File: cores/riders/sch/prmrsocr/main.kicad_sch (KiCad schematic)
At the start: 31 parts

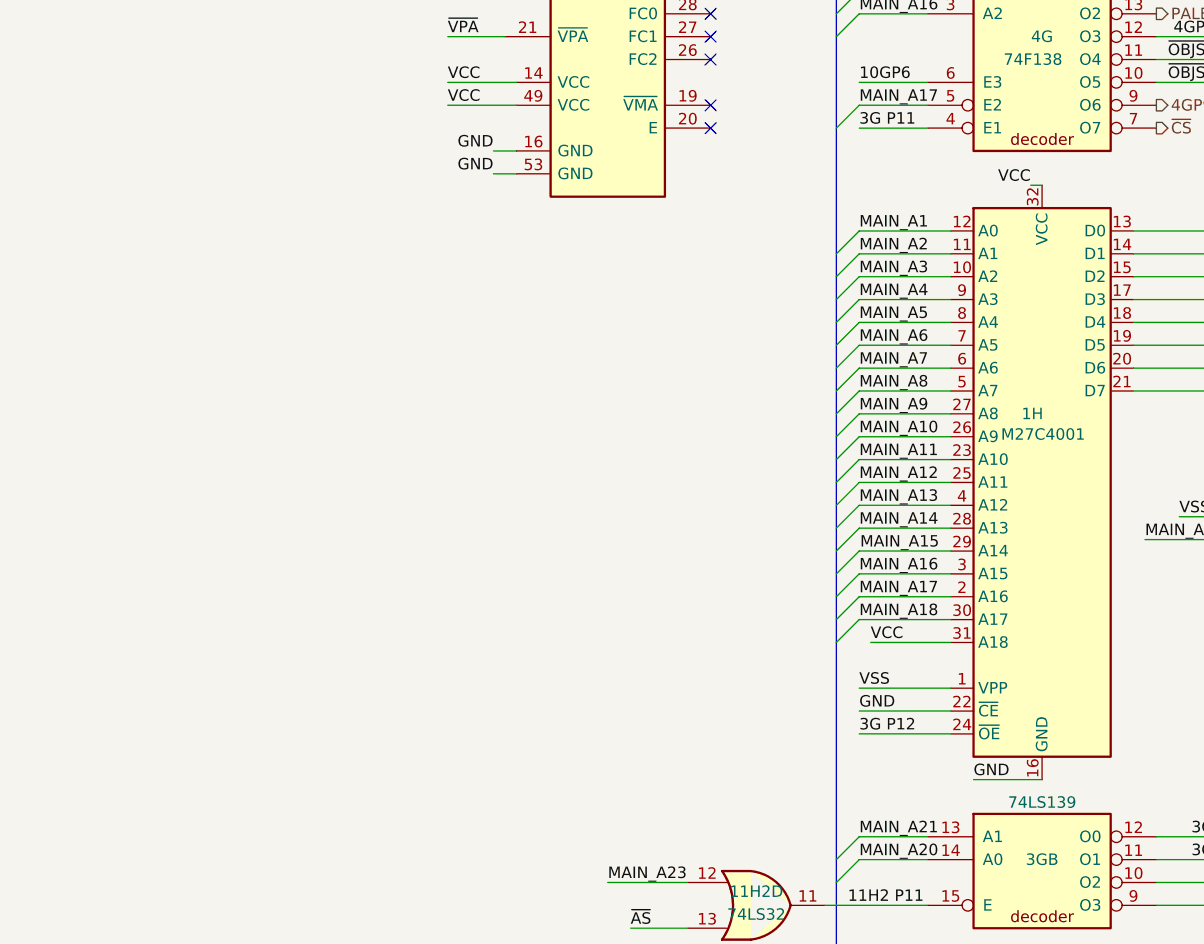
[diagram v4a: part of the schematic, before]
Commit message: prmrsocr sch: finish remove errors
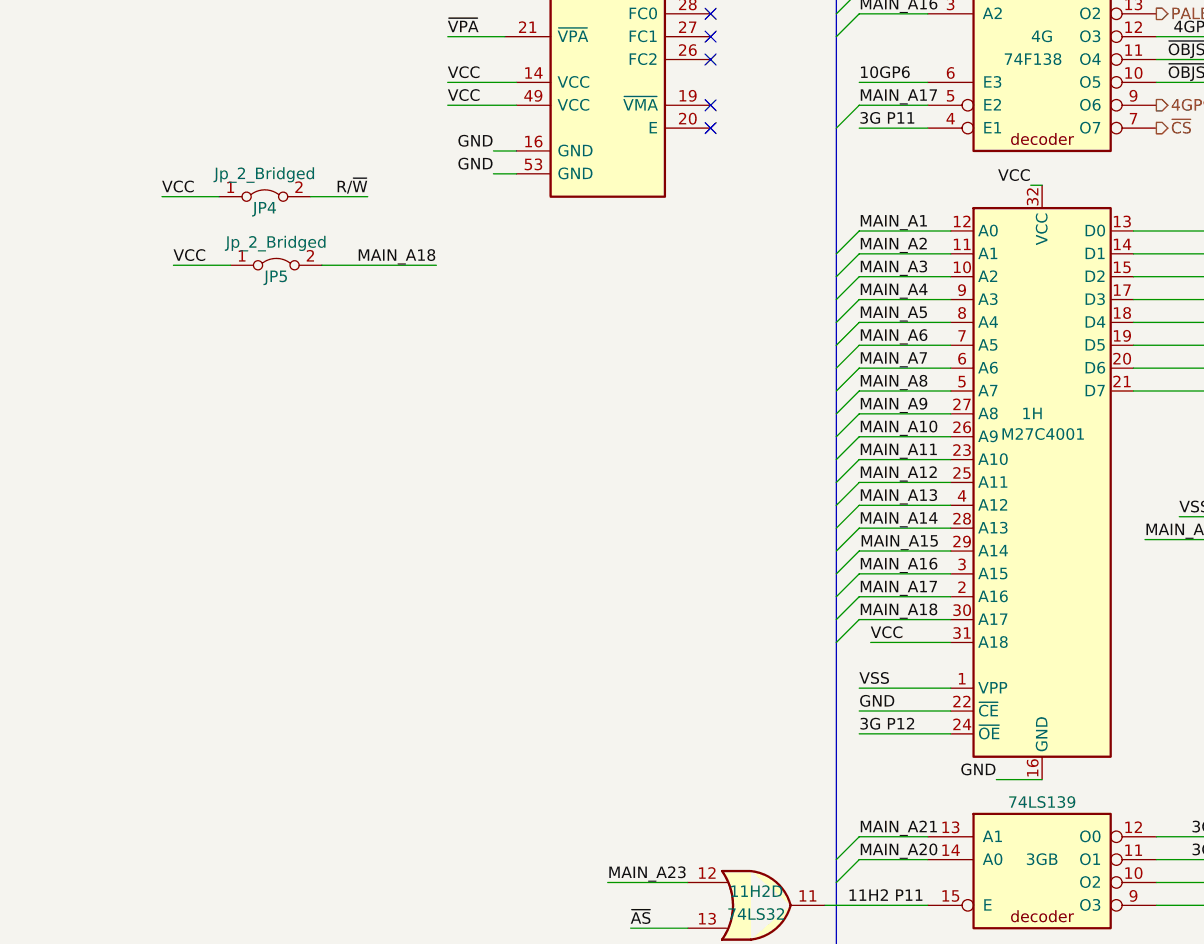
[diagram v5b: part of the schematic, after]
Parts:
- added JP4, JP5: Jp_2_Bridged, symbol Jumper:Jumper_2_Bridged
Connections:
- net MAIN_A18: now also JP5.2 (B)
- net R/~{W}: now also JP4.2 (B)
- net VCC: now also JP4.1 (A), JP5.1 (A)
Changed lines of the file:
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@@
 	(wire
 		(pts
+			(xy 280.67 132.08) (xy 267.97 132.08)
+		)
+		(stroke
+			(width 0)
+			(type default)
+		)
+	)
+	(wire
+		(pts
 			(xy 210.82 52.07) (xy 203.2 52.07)
 		)
@@
 		)
 	)
+	(wire
+		(pts
+			(xy 250.19 124.46) (xy 256.54 124.46)
+		)
+		(stroke
+			(width 0)
+			(type default)
+		)
+	)
 	(bus
 		(pts
@@
 	(wire
 		(pts
-			(xy 340.36 189.23) (xy 347.98 189.23)
-		)
-		(stroke
-			(width 0)
-			(type default)
-		)
-	)
-	(wire
-		(pts
 			(xy 273.05 45.72) (xy 288.29 45.72)
 		)
@@
 	(wire
 		(pts
+			(xy 273.05 124.46) (xy 266.7 124.46)
+		)
+		(stroke
+			(width 0)
+			(type default)
+		)
+	)
+	(wire
+		(pts
 			(xy 43.18 81.28) (xy 53.34 81.28)
 		)
@@
 		)
 	)
+	(wire
+		(pts
+			(xy 251.46 132.08) (xy 257.81 132.08)
+		)
+		(stroke
+			(width 0)
+			(type default)
+		)
+	)
 	(bus
 		(pts
@@
 	(wire
 		(pts
+			(xy 342.9 189.23) (xy 347.98 189.23)
+		)
+		(stroke
+			(width 0)
+			(type default)
+		)
+	)
+	(wire
+		(pts
 			(xy 337.82 148.59) (xy 327.66 148.59)
 		)
@@
 		)
 	)
+	(label "VCC"
+		(at 250.19 124.46 0)
+		(effects
+			(font
+				(size 1.27 1.27)
+			)
+			(justify left bottom)
+		)
+	)
 	(label "MAIN_A7"
 		(at 157.48 231.14 0)
@@
 		)
 	)
-	(label "GND"
-		(at 340.36 189.23 0)
+	(label "MAIN_D5"
+		(at 43.18 161.29 0)
 		(effects
 			(font
@@
 		)
 	)
-	(label "MAIN_D5"
-		(at 43.18 161.29 0)
+	(label "VCC"
+		(at 251.46 132.08 0)
 		(effects
 			(font
@@
 		)
 	)
+	(label "MAIN_A18"
+		(at 280.67 132.08 180)
+		(effects
+			(font
+				(size 1.27 1.27)
+			)
+			(justify right bottom)
+		)
+	)
 	(label "MAIN_A16"
 		(at 327.66 166.37 0)
@@
 		)
 	)
+	(label "R{slash}~{W}"
+		(at 273.05 124.46 180)
+		(effects
+			(font
+				(size 1.27 1.27)
+			)
+			(justify right bottom)
+		)
+	)
 	(label "VSS"
 		(at 260.35 250.19 0)
@@
 		)
 	)
+	(label "GND"
+		(at 342.9 189.23 180)
+		(effects
+			(font
+				(size 1.27 1.27)
+			)
+			(justify right bottom)
+		)
+	)
 	(label "~{HALT}"
 		(at 280.67 88.9 0)
@@
 	)
 	(symbol
+		(lib_id "Jumper:Jumper_2_Bridged")
+		(at 261.62 124.46 0)
+		(unit 1)
+		(exclude_from_sim no)
+		(in_bom yes)
+		(on_board yes)
+		(dnp no)
+		(property "Reference" "JP4"
+			(at 261.62 125.73 0)
+			(effects
+				(font
+					(size 1.27 1.27)
+				)
+			)
+		)
+		(property "Value" "Jp_2_Bridged"
+			(at 261.62 121.92 0)
+			(effects
+				(font
+					(size 1.27 1.27)
+				)
+			)
+		)
+		(property "Footprint" ""
+			(at 261.62 124.46 0)
+			(effects
+				(font
+					(size 1.27 1.27)
+				)
+				(hide yes)
+			)
+		)
+		(property "Datasheet" "~"
+			(at 261.62 124.46 0)
+			(effects
+				(font
+					(size 1.27 1.27)
+				)
+				(hide yes)
+			)
+		)
+		(property "Description" ""
+			(at 261.62 124.46 0)
+			(effects
+				(font
+					(size 1.27 1.27)
+				)
+				(hide yes)
+			)
+		)
+		(pin "1"
+		)
+		(pin "2"
+		)
+		(instances
+			(project "prmrsocr"
+				(path "/0011ec10-82c4-4039-b424-337480f568e8/7d4ab3ba-37fa-4111-bbdb-c99f1a708a52"
+					(reference "JP4")
+					(unit 1)
+				)
+			)
+		)
+	)
+	(symbol
 		(lib_id "Memory_EPROM:27C040")
 		(at 347.98 60.96 0)
@@
 				)
 			)
+		)
+	)
+	(symbol
+		(lib_id "Jumper:Jumper_2_Bridged")
+		(at 262.89 132.08 0)
+		(unit 1)
+		(exclude_from_sim no)
+		(in_bom yes)
+		(on_board yes)
+		(dnp no)
+		(property "Reference" "JP5"
+			(at 262.89 133.35 0)
+			(effects
+				(font
+					(size 1.27 1.27)
+				)
+			)
+		)
+		(property "Value" "Jp_2_Bridged"
+			(at 262.89 129.54 0)
+			(effects
+				(font
+					(size 1.27 1.27)
+				)
+			)
+		)
+		(property "Footprint" ""
+			(at 262.89 132.08 0)
+			(effects
+				(font
+					(size 1.27 1.27)
+				)
+				(hide yes)
+			)
+		)
+		(property "Datasheet" "~"
+			(at 262.89 132.08 0)
+			(effects
+				(font
+					(size 1.27 1.27)
+				)
+				(hide yes)
+			)
+		)
+		(property "Description" ""
+			(at 262.89 132.08 0)
+			(effects
+				(font
+					(size 1.27 1.27)
+				)
+				(hide yes)
+			)
+		)
+		(pin "1"
+		)
+		(pin "2"
+		)
+		(instances
+			(project "prmrsocr"
+				(path "/0011ec10-82c4-4039-b424-337480f568e8/7d4ab3ba-37fa-4111-bbdb-c99f1a708a52"
+					(reference "JP5")
+					(unit 1)
+				)
+			)

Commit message: prmrsocr sch corrections
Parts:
- removed 13H, 14H: 74LS245, symbol jt74:74LS245
- removed 15A: ER5911, symbol arcade:ER5911
- removed 15C2: 74LS174, symbol jt74:74LS174
- removed 16C: 74LS273, symbol jt74:74LS273
- removed 7E1: 74LS32, symbol jt74:74LS32
- removed unit 1 of 7G
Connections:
- net 3G P12 renamed ~{ROM_CS}
- net 3GA P4 renamed 3GP4
- net 4GP15 renamed ~{RAM_CS}
- net 4GP9 renamed ~{NWCS}
- net 7E2 P13 renamed 7E2P13
- net ~{CS} renamed ~{PCU_CS}
- net ~{P1401} renamed ~{OBJ_CS}
- no-connect marks 28 -> 22
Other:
- moved on the sheet: 10GC, 10GE, 11G1C, 11G1D, 11H1A, 11H1B, 11H2D, 12HB, 12HD, 15H2D, 16HA, 16HB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

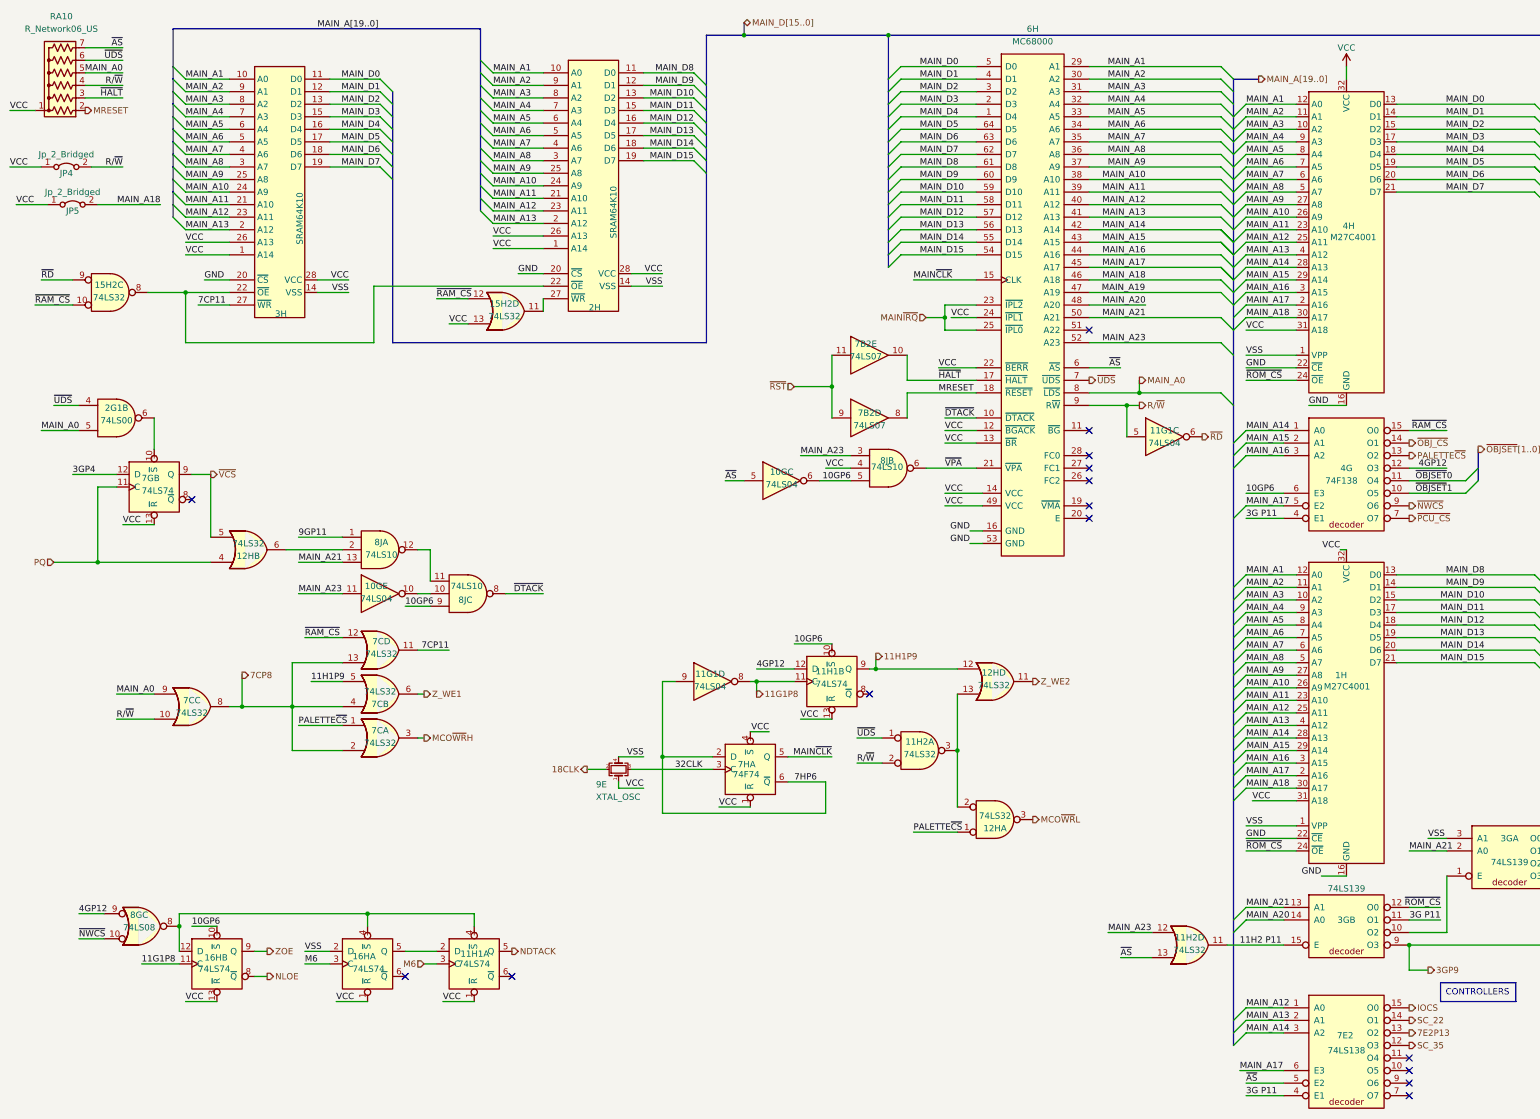
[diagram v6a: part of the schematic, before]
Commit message: Adding Konami Asic to prmrsocr
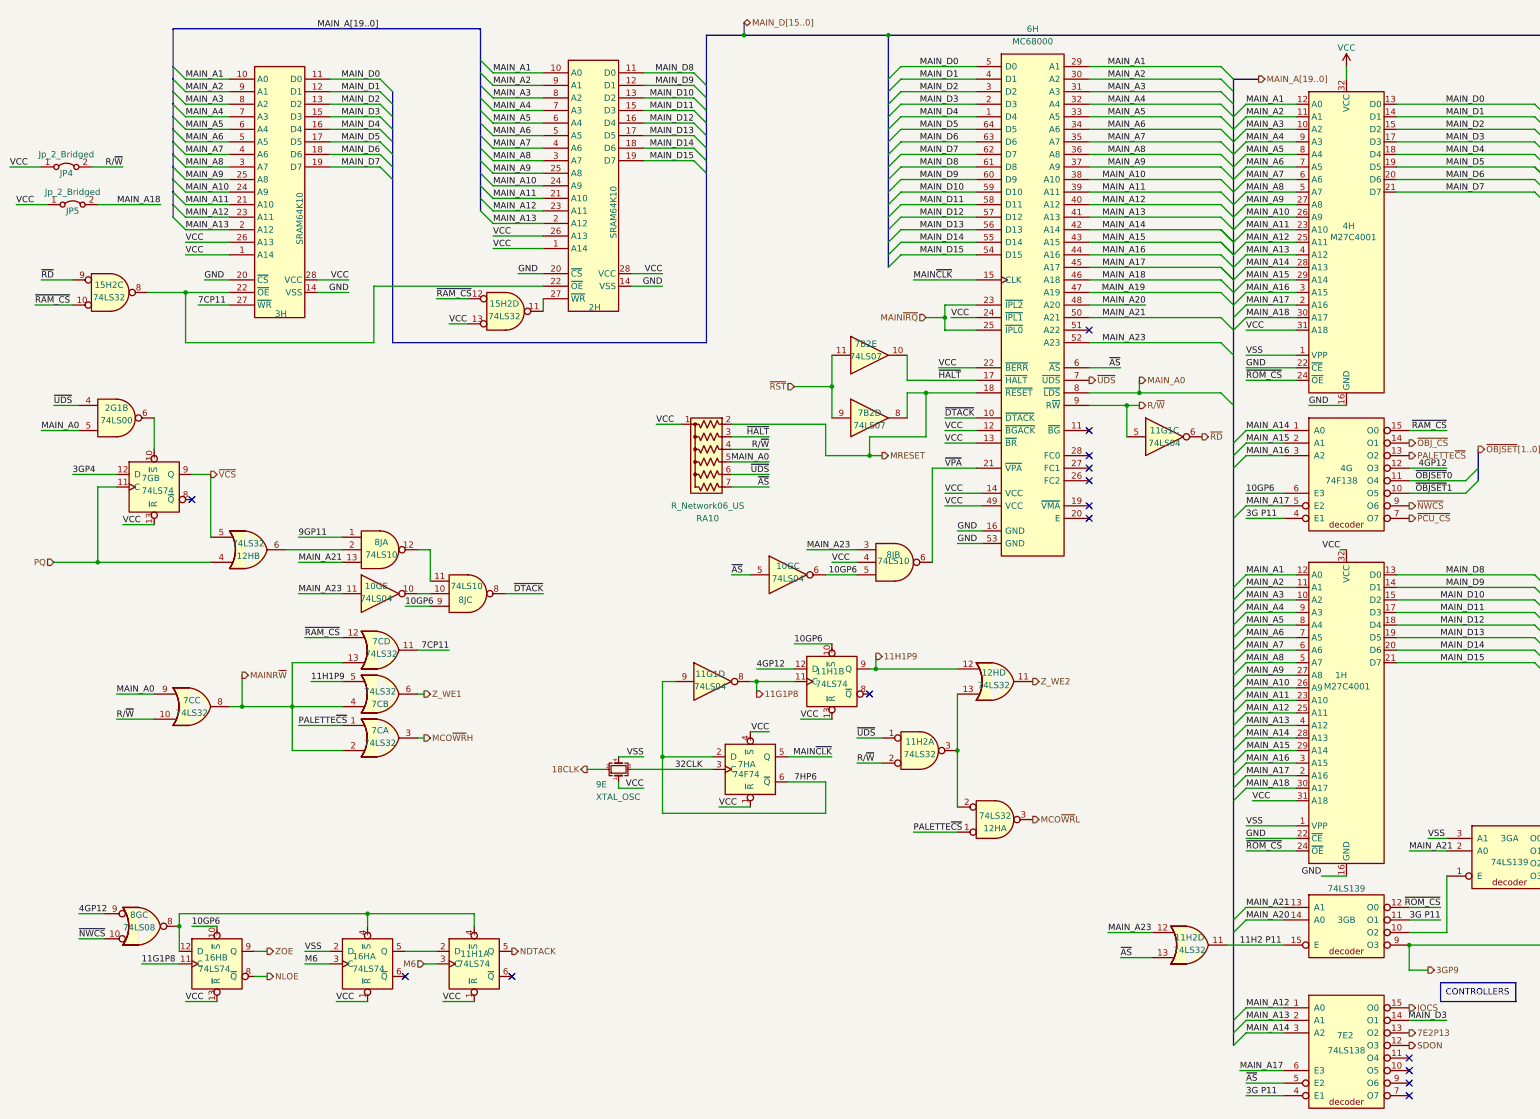
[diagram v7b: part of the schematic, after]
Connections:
- net SC_22 is gone; now on net MAIN_D3: 7E2.14 (O1)
- net GND: now also 2H.14 (VSS), 3H.14 (VSS)
- net VSS: no longer 2H.14 (VSS), 3H.14 (VSS)
- net 7CP8 renamed MAINR~{W}
- net SC_35 renamed SDON
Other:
- moved on the sheet: 10GC, 8JB, RA10
